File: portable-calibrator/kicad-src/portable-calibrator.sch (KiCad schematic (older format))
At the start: 15 parts, among them J1 Conn_01x02, J2 Conn_01x02, Q1 MMBT3904-7-F, U1 LM399, U2 LT1012

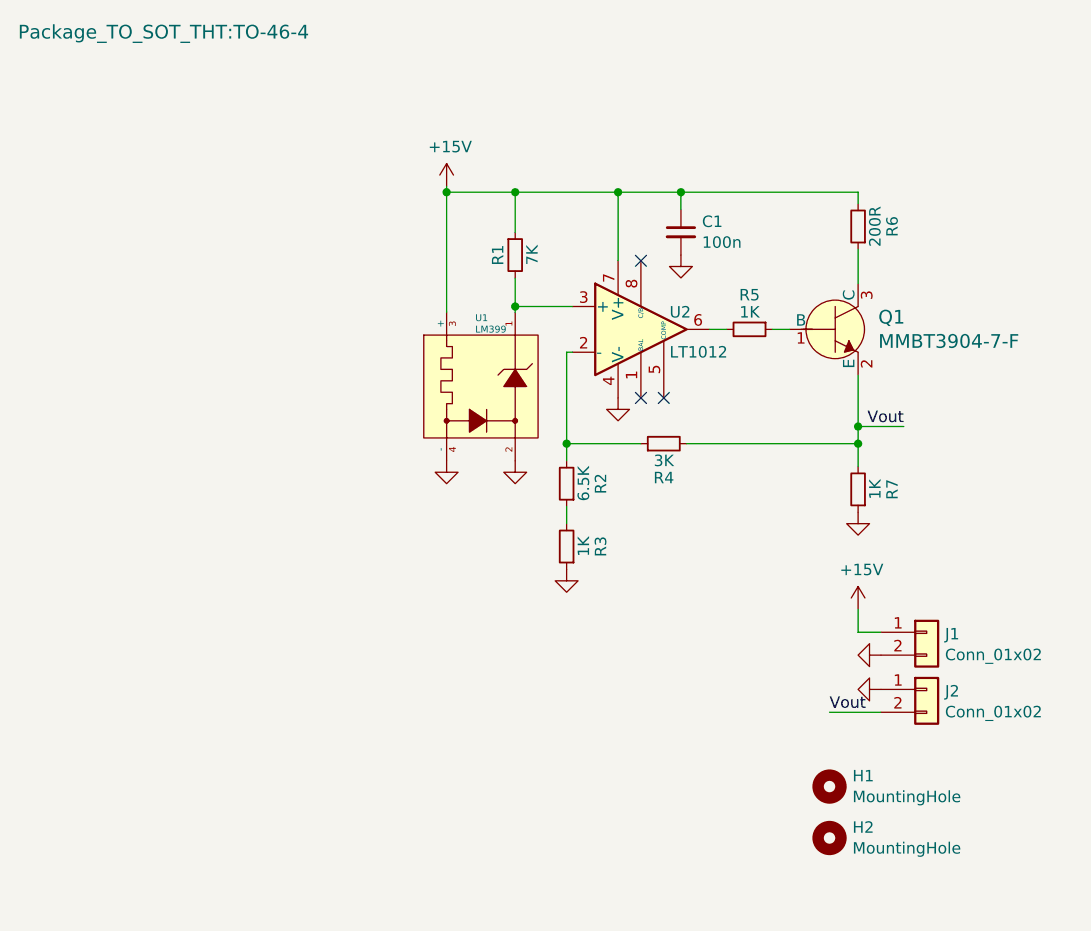
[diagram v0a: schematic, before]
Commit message: reroute portable calibrator
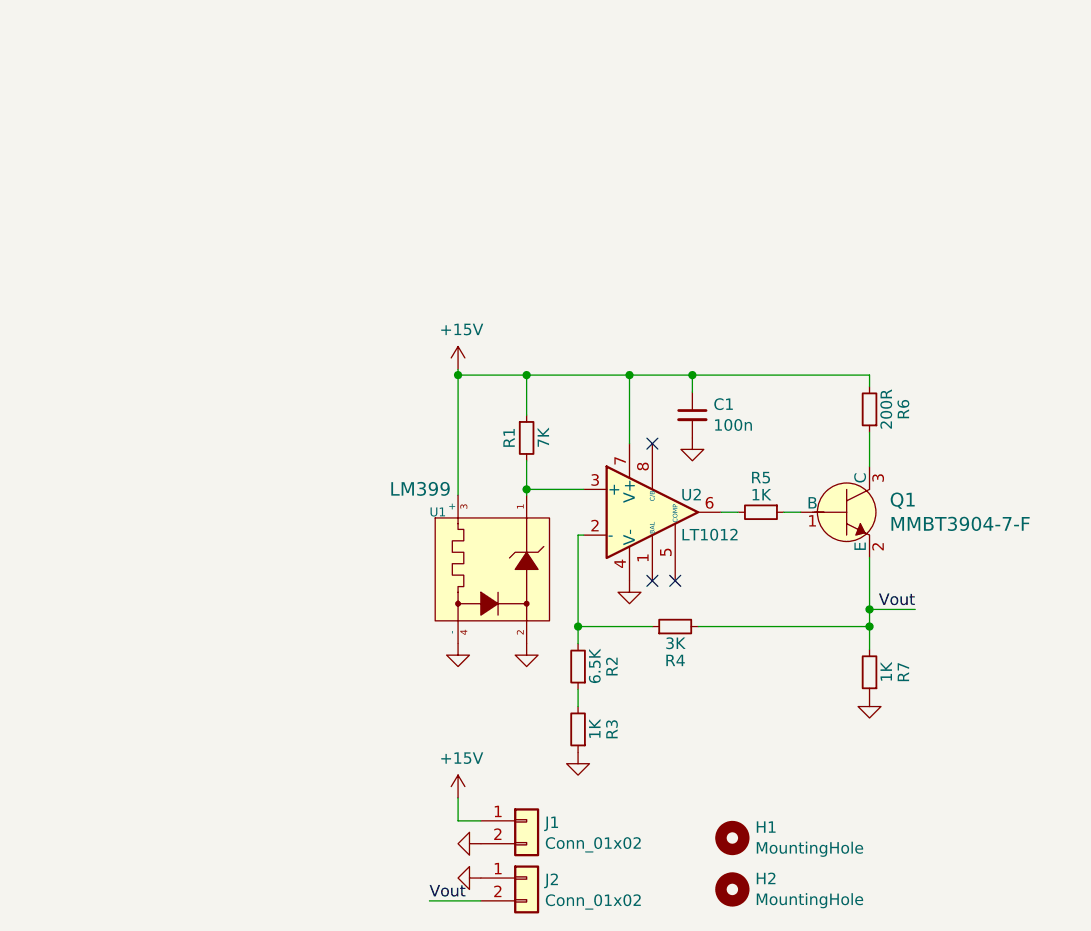
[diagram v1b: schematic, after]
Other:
- moved on the sheet: C1, H1, H2, J1, J2, Q1, R1, R2, R3, R4, R5, R6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
